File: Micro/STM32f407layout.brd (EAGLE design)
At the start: 100.1 x 96.7 mm, 68 parts, among them Q1 ASF, Q2 ASV-8, T3 FDN340P, T4 AP1117_LIN_REG

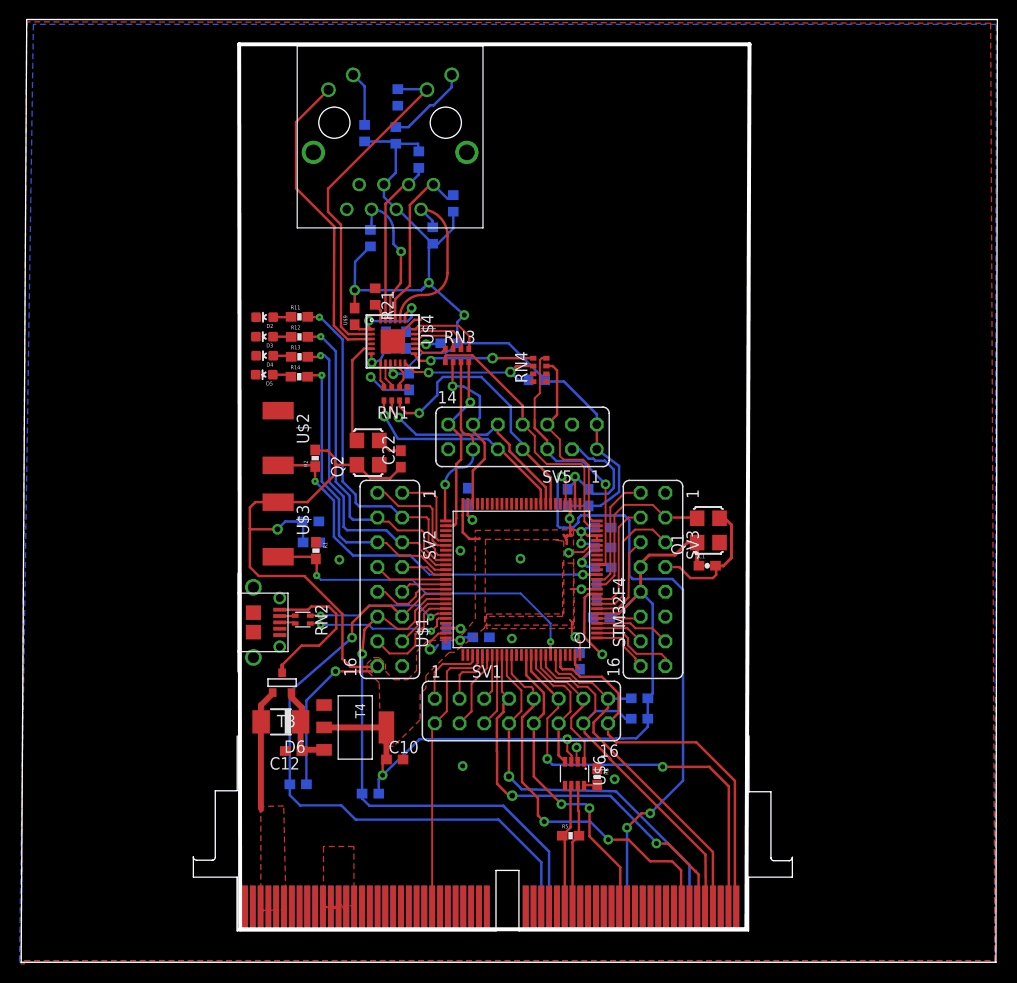
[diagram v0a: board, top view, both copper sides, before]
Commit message: Fixed some wiring on the microboard
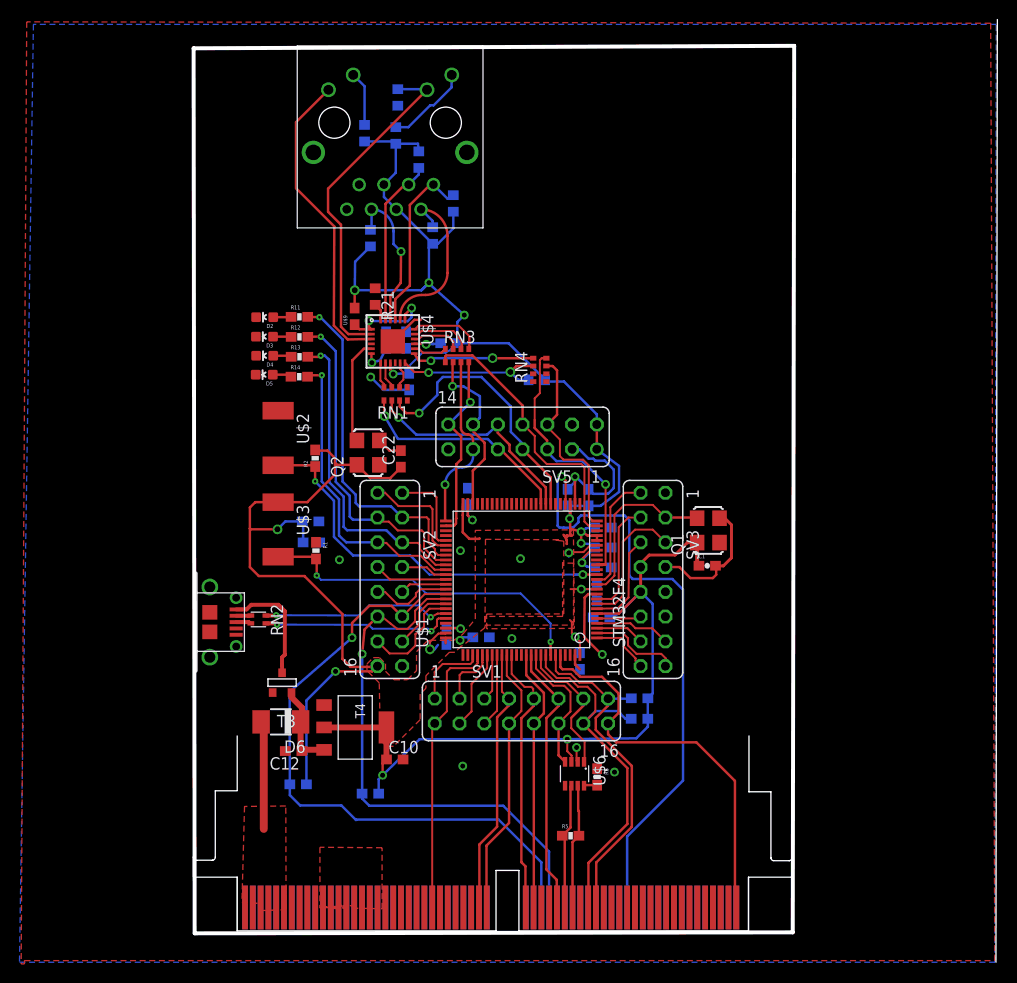
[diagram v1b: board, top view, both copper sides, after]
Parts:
- moved RN2 4.55 mm to (24.3, 35.2)
- moved U$5 4.47 mm to (17.9, 34.9)
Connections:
- net +5V: now also U$8.T1, U$8.T2
- net GND: now also U$8.T16, U$8.T17, U$8.T18
- net I2C1_SCL: now also U$8.T42; no longer U$8.T57
- net I2C1_SDA: now also U$8.T41; no longer U$8.T56
- net MAIN_CAMERA_SERVO_MOTOR_PWM: now also U$8.T37; no longer U$8.T59
- net SHIFTREG_CLK: now also U$8.T32; no longer U$8.B54
- net SHIFTREG_DATA: now also U$8.T33; no longer U$8.T53
- net SHIFTREG_ENABLE: now also U$8.T31; no longer U$8.T55
- net SONAR_PWM: now also U$8.T34, U$8.T40; no longer U$8.T45
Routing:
- net MAIN_CAMERA_SERVO_MOTOR_PWM: track 44.6 -> 28.0 mm, vias 2 -> 0
- net SHIFTREG_ENABLE: track 42.1 -> 27.5 mm, vias 2 -> 0
- net SHIFTREG_CLK: track 40.2 -> 28.0 mm, vias 1 -> 0
- net SHIFTREG_DATA: track 39.8 -> 28.0 mm, vias 2 -> 0
- net SONAR_PWM: track 32.2 -> 27.1 mm, vias 2 -> 0
- net USB_D+: track 15.1 -> 19.7 mm
- net USB_D-: track 14.9 -> 19.5 mm
- net N$57: track 15.6 -> 11.9 mm
- net I2C1_SCL: track 37.7 -> 35.6 mm
- net I2C1_SDA: track 40.8 -> 39.1 mm
- net +5V: track 12.9 -> 11.3 mm
- net SONAR_DAC: track 64.0 -> 63.4 mm, vias 3 -> 1
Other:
- board size 100.1 x 96.7 mm -> 82.5 x 96.7 mm

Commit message: Cleaned up the board
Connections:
- net SONAR_PWM: no longer U$8.T40
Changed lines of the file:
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@@
 <?xml version="1.0" encoding="utf-8"?>
 <!DOCTYPE eagle SYSTEM "eagle.dtd">
-<eagle version="7.5.0">
+<eagle version="7.2.0">
 <drawing>
 <settings>
@@
 <wire x1="52.58884375" y1="24.503040625" x2="52.58884375" y2="5.6464625" width="0.254" layer="1"/>
 <wire x1="52.58884375" y1="5.6464625" x2="52.563659375" y2="5.621278125" width="0.254" layer="1"/>
-<contactref element="U$8" pad="T40"/>
-<wire x1="52.58884375" y1="5.6464625" x2="57.363659375" y2="5.621278125" width="0" layer="19" extent="1-1"/>
 </signal>
 <signal name="I2C1_SDA">

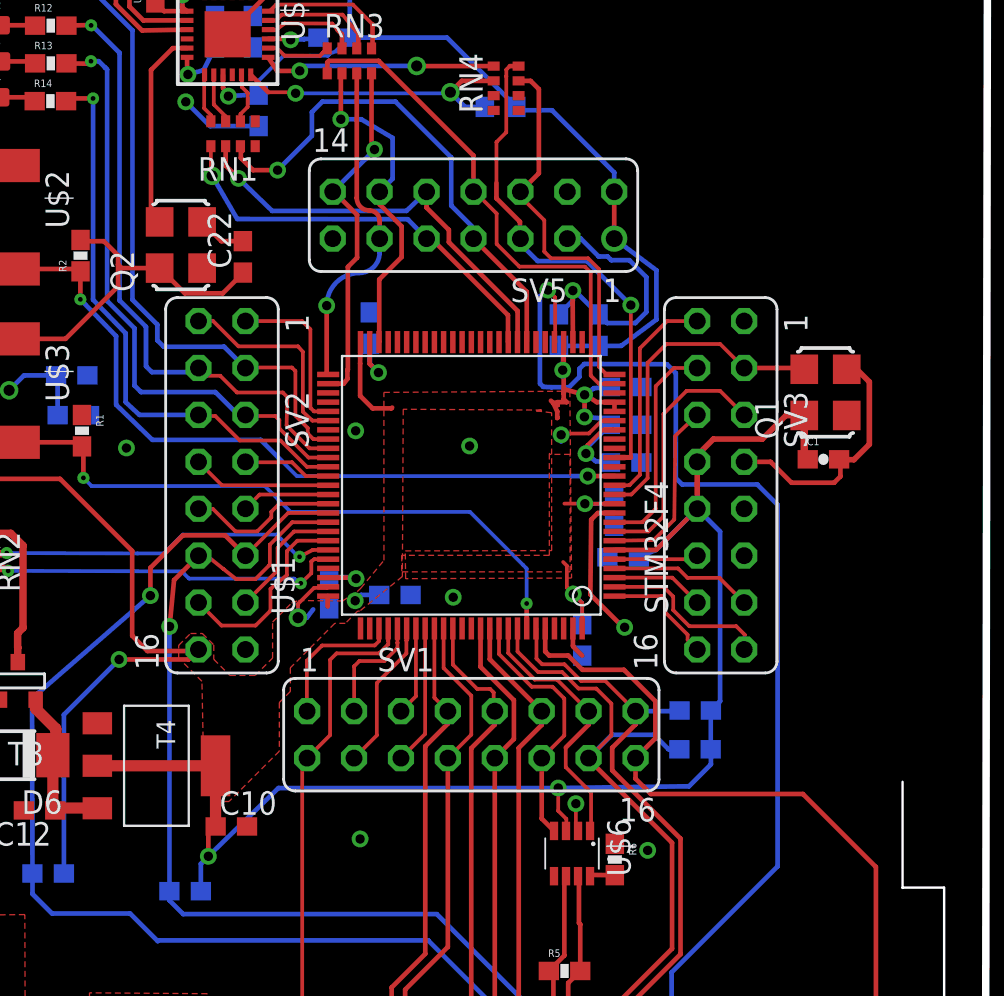
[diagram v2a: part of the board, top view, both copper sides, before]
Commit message: Added Silkscreen Pin labels
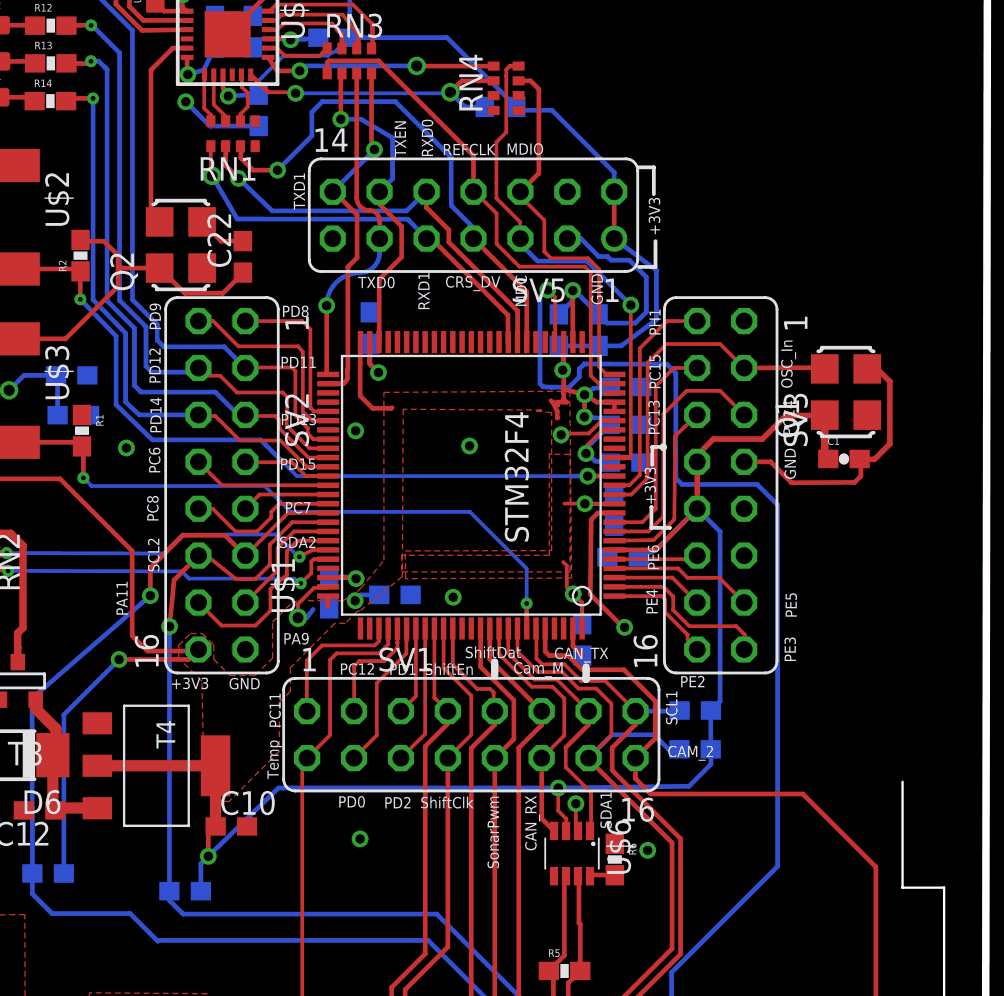
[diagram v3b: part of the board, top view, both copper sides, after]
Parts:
- moved C1 1.11 mm to (71.5, 40.7)
- moved Q1 1.11 mm to (71.6, 44.3)
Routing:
- net +3V3: track 288.8 -> 289.9 mm
- net GND: track 61.6 -> 62.7 mm
- net OSC_IN: track 17.9 -> 19.0 mm
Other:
- board text added: "+3V3"
- board text added: "CAM_2"
- board text added: "CAN_RX"
- board text added: "CAN_TX"
- board text added: "CRS_DV"
- board text added: "Cam_M"
- board text added: "GND"
- board text added: "MDC"
- board text added: "MDIO"
- board text added: "OSC_In"
- board text added: "PA11"
- board text added: "PA9"
- board text added: "PC11"
- board text added: "PC12"
- board text added: "PC13"
- board text added: "PC14"
- board text added: "PC15"
- board text added: "PC6"
- board text added: "PC7"
- board text added: "PC8"
- board text added: "PD0"
- board text added: "PD1"
- board text added: "PD11"
- board text added: "PD12"
- board text added: "PD13"
- board text added: "PD14"
- board text added: "PD15"
- board text added: "PD2"
- board text added: "PD8"
- board text added: "PD9"
- board text added: "PE2"
- board text added: "PE3"
- board text added: "PE4"
- board text added: "PE5"
- board text added: "PE6"
- board text added: "PH1"
- board text added: "REFCLK"
- board text added: "RXD0"
- board text added: "RXD1"
- board text added: "SCL1"
- board text added: "SCL2"
- board text added: "SDA1"
- board text added: "SDA2"
- board text added: "ShiftClk"
- board text added: "ShiftDat"
- board text added: "ShiftEn"
- board text added: "SonarPwm"
- board text added: "TXD0"
- board text added: "TXD1"
- board text added: "TXEN"
- board text added: "Temp"
